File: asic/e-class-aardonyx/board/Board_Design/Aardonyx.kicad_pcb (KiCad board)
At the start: 4 copper layers, 311 parts, among them J1 USB_B_6PIN, J10 Conn_1x6_F, J11 Conn_1x6_F, J12 Conn_1x3_M, J13 Conn_1x8_F, J14 Conn_1x6_F, J15 Conn_1x10, J16 Conn_1x8_F, J17 USB_OTG, J18 Conn_1x3_M, J19 Conn_1x3_M, J2 Conn_1x8, J3 Conn_1x3_M, J4 Conn_1x4, J5 PJ-202H PWRJACK, J6 Conn_1x3_M, J7 Conn_1x4, J8 Conn_1x3_M, J9 Conn_1x8, Q1 FDN339AN, SW1 SW_SPST, SW2 FSM2JSMAATR, SW3 SW_DIP_x03, U1 FT2232H, U10 TPS7A7002DDAR, U11 ADM1085, U12 ADM1085, U13 TPS7A7002DDAR, U14 74AUP1G09GW, U15 SKT32E, U16 93LC56BT-I_OT, U2 IS42S32160F-TSOP2, U3 CDCE913PW, U4 TPS54627DDAR, U5 CAT24M01WI-GT3, U6 IS25LP256x-xM, U7 ADC128S102CIMTX/NOPB, U8 LSF0108PWR, U9 LSF0108PWR, Y1 12MHz, Y2 27MHz

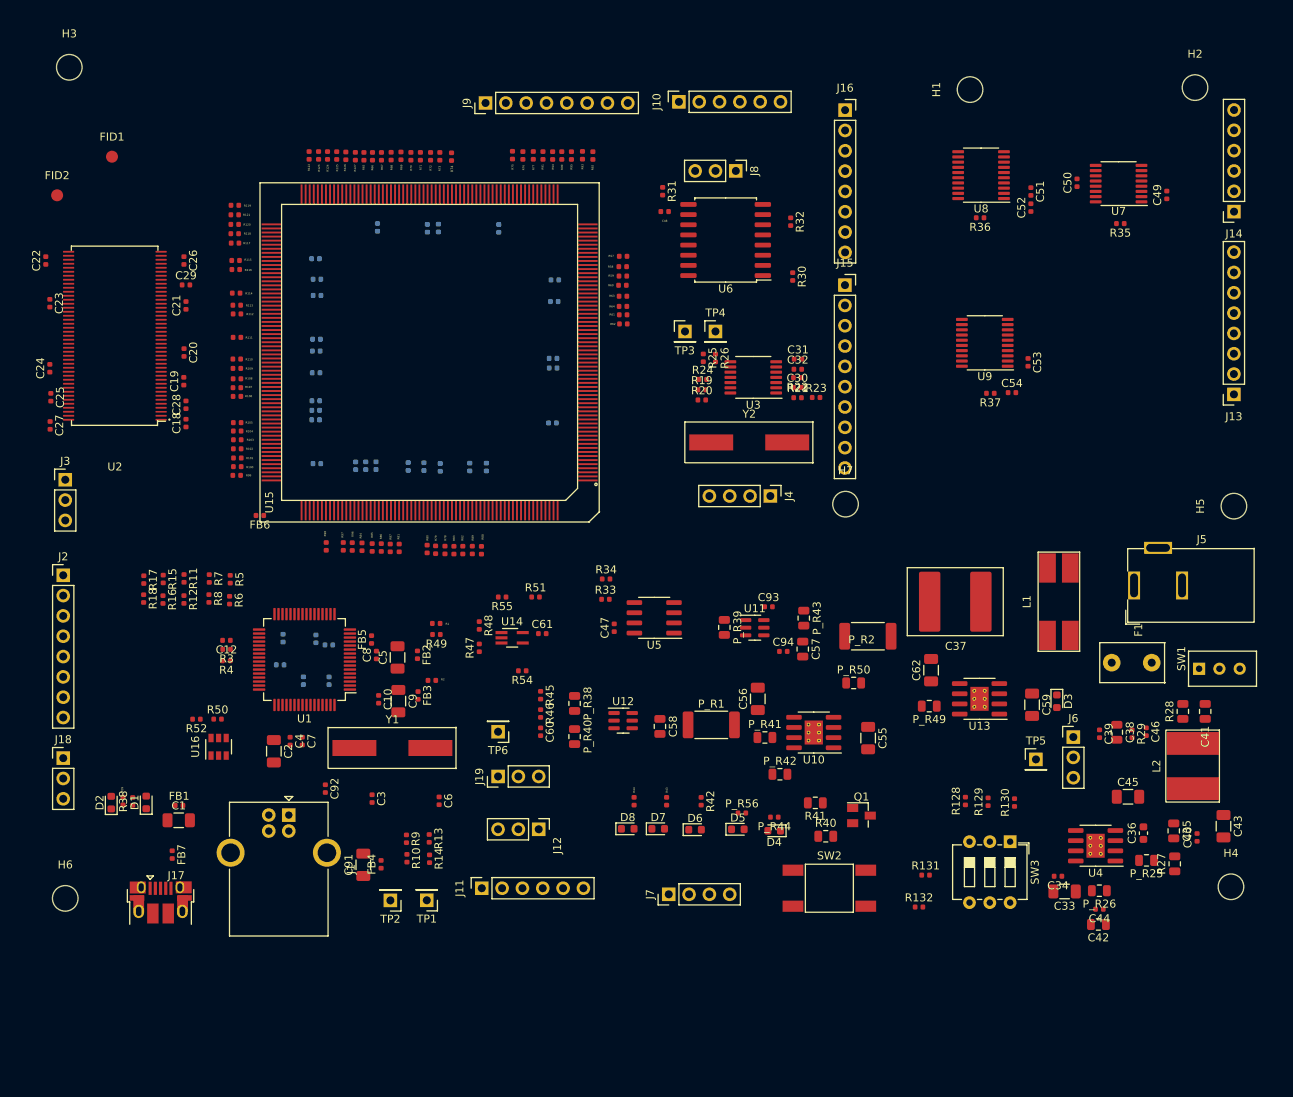
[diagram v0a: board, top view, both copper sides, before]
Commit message: minimize pcb size
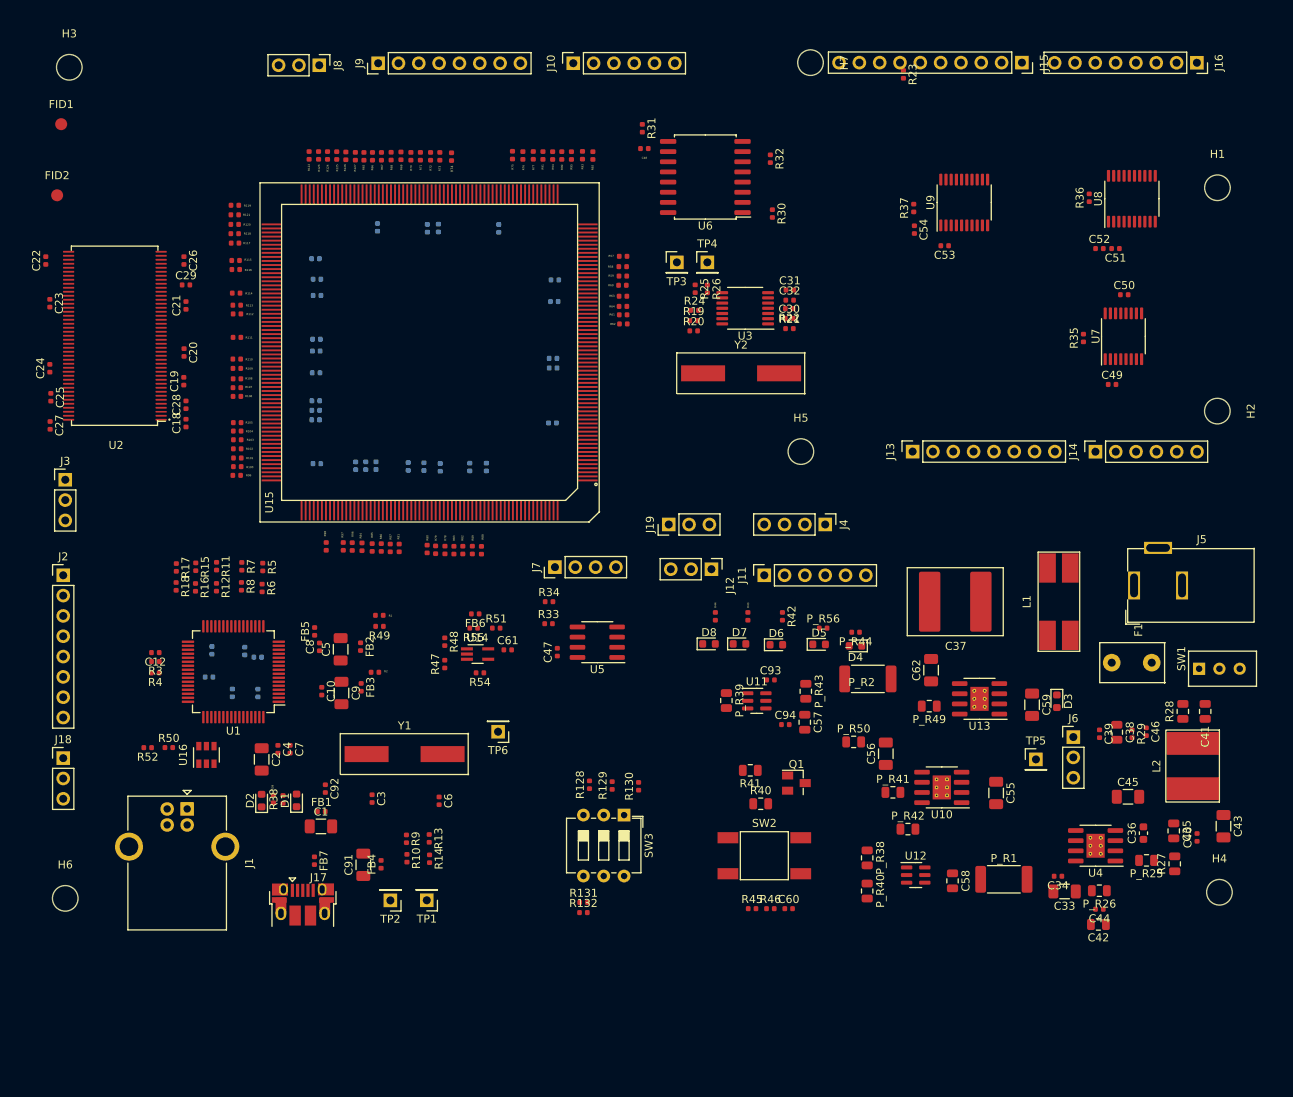
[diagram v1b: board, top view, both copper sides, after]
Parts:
- moved H7 55.4 mm to (222.4, 51.0), turned to 270 degrees
- moved H5 54.6 mm to (221.2, 99.6), turned to 0 degrees
- moved J8 53.7 mm to (161.0, 51.3)
- moved J11 52.7 mm to (216.7, 115.1)
- moved SW3 48.4 mm to (199.1, 145.0)
- moved R129 47.0 mm to (197.7, 141.3)
- moved R130 47.0 mm to (201.0, 141.4)
- moved R128 47.0 mm to (194.8, 141.2)
- moved J16 44.4 mm to (270.7, 51.0), turned to 270 degrees
- moved J7 43.3 mm to (190.5, 114.0)
- moved R131 42.9 mm to (194.1, 156.0)
- moved R132 42.0 mm to (194.1, 157.2)
- moved R23 41.8 mm to (234.1, 52.5), turned to 270 degrees
- moved U12 41.4 mm to (235.6, 152.5)
- moved P_R1 41.4 mm to (246.6, 153.1)
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
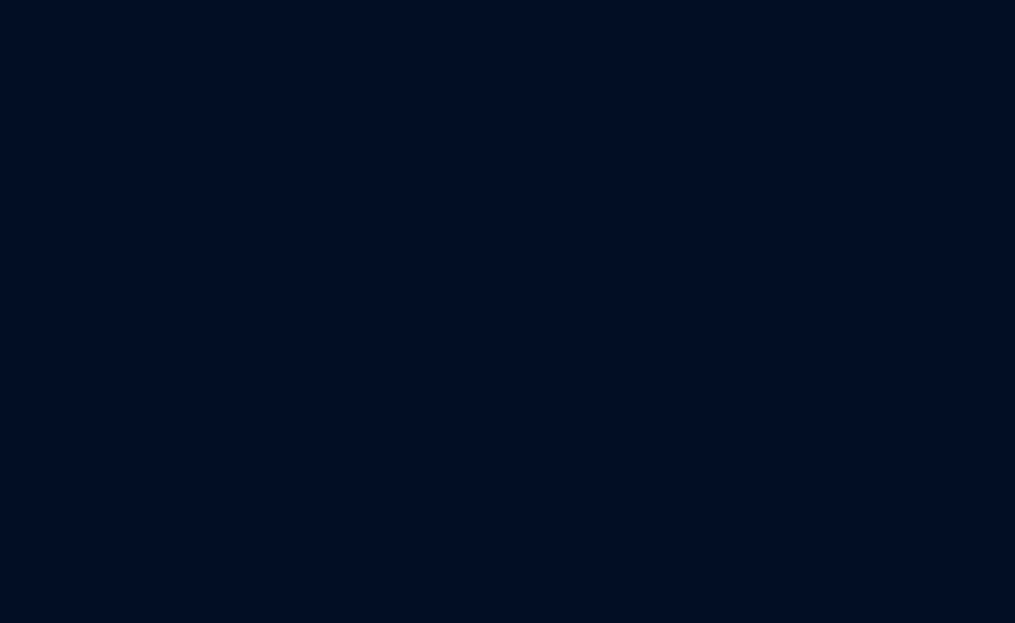
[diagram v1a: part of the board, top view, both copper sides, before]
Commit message: Updating footprint for test points
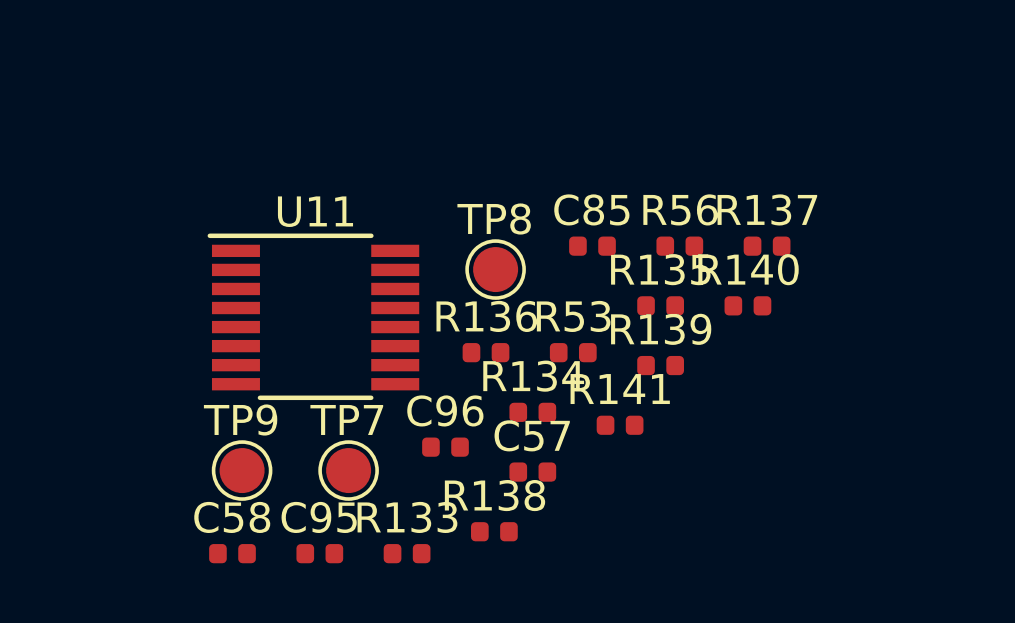
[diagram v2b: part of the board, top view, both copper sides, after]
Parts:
- added C57: 0.1UF,0402, Capacitor_SMD:C_0402_1005Metric, F.Cu at (160.5, 175.3)
- added C58: 0.1UF,0402, Capacitor_SMD:C_0402_1005Metric, F.Cu at (150.5, 178.0)
- added C85: 0.1UF,0402, Capacitor_SMD:C_0402_1005Metric, F.Cu at (162.5, 167.7)
- added C95: 0.1UF,0402, Capacitor_SMD:C_0402_1005Metric, F.Cu at (153.4, 178.0)
- added C96: 0.1UF,0402, Capacitor_SMD:C_0402_1005Metric, F.Cu at (157.6, 174.4)
- added R133: 4.7KE,0402, Resistor_SMD:R_0402_1005Metric, F.Cu at (156.3, 178.0)
- added R134: 1.2kE, 0402, Resistor_SMD:R_0402_1005Metric, F.Cu at (160.5, 173.3)
- added R135: 1.2kE, 0402, Resistor_SMD:R_0402_1005Metric, F.Cu at (164.8, 169.7)
- added R136: 4.7KE,0402, Resistor_SMD:R_0402_1005Metric, F.Cu at (159.0, 171.3)
- added R137: 10KE,0402, Resistor_SMD:R_0402_1005Metric, F.Cu at (168.3, 167.7)
- added R138: 10KE,0402, Resistor_SMD:R_0402_1005Metric, F.Cu at (159.2, 177.2)
- added R139: 10KE,0402, Resistor_SMD:R_0402_1005Metric, F.Cu at (164.8, 171.7)
- added R140: 10KE,0402, Resistor_SMD:R_0402_1005Metric, F.Cu at (167.7, 169.7)
- added R141: 10KE,0402, Resistor_SMD:R_0402_1005Metric, F.Cu at (163.4, 173.7)
- added R53: 4.7KE,0402, Resistor_SMD:R_0402_1005Metric, F.Cu at (161.9, 171.3)
- added R56: 3.3kE, 0402, Resistor_SMD:R_0402_1005Metric, F.Cu at (165.4, 167.7)
- added TP7: OUT3, TestPoint:TestPoint_Pad_D1.5mm, F.Cu at (154.4, 175.2)
- added TP8: OUT4, TestPoint:TestPoint_Pad_D1.5mm, F.Cu at (159.3, 168.5)
- added TP9: POWER_GOOD, TestPoint:TestPoint_Pad_D1.5mm, F.Cu at (150.8, 175.2)
- added U11: ADM1186, Package_SO:QSOP-16_3.9x4.9mm_P0.635mm, F.Cu at (153.3, 170.1)
- R19, R20, R21, R22, R23, R45: value 4.7KE, 0402 -> 4.7KE,0402
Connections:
- R49 pad 1: /ftdi/RESET -> /RESET
- R54 pad 2: /power_2/RESET -> /RESET
- R55 pad 2: /power_2/RESET -> /RESET
- U15 pad 24: /power_2/RESET -> /RESET

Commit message: add bom & updated component
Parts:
- R40, R41: footprint Resistor_SMD:R_0805_2012Metric -> Resistor_SMD:R_0402_1005Metric
- TP1, TP2, TP3, TP4, TP5, TP6: footprint Connector_PinHeader_2.54mm:PinHeader_1x01_P2.54mm_Vertical -> TestPoint:TestPoint_Pad_D1.5mm
- moved C42 44.9 mm to (234.9, 120.4)
- moved R139 41.1 mm to (192.0, 141.0)
- moved C44 41.0 mm to (235.5, 122.9)
- moved R53 40.6 mm to (188.0, 140.3)
- moved C85 40.1 mm to (188.9, 137.5)
- moved R135 40.1 mm to (191.2, 139.5)
- moved R137 40.1 mm to (194.8, 137.5)
- moved R140 40.1 mm to (194.1, 139.5)
- moved R56 40.1 mm to (191.8, 137.5)
- moved R134 39.4 mm to (192.3, 149.9)
- moved U11 39.4 mm to (185.0, 146.7)
- moved C57 39.4 mm to (192.3, 151.9)
- moved C58 39.4 mm to (182.3, 154.6)
- moved C95 39.4 mm to (185.2, 154.6)
- moved C96 39.4 mm to (189.4, 151.1)
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
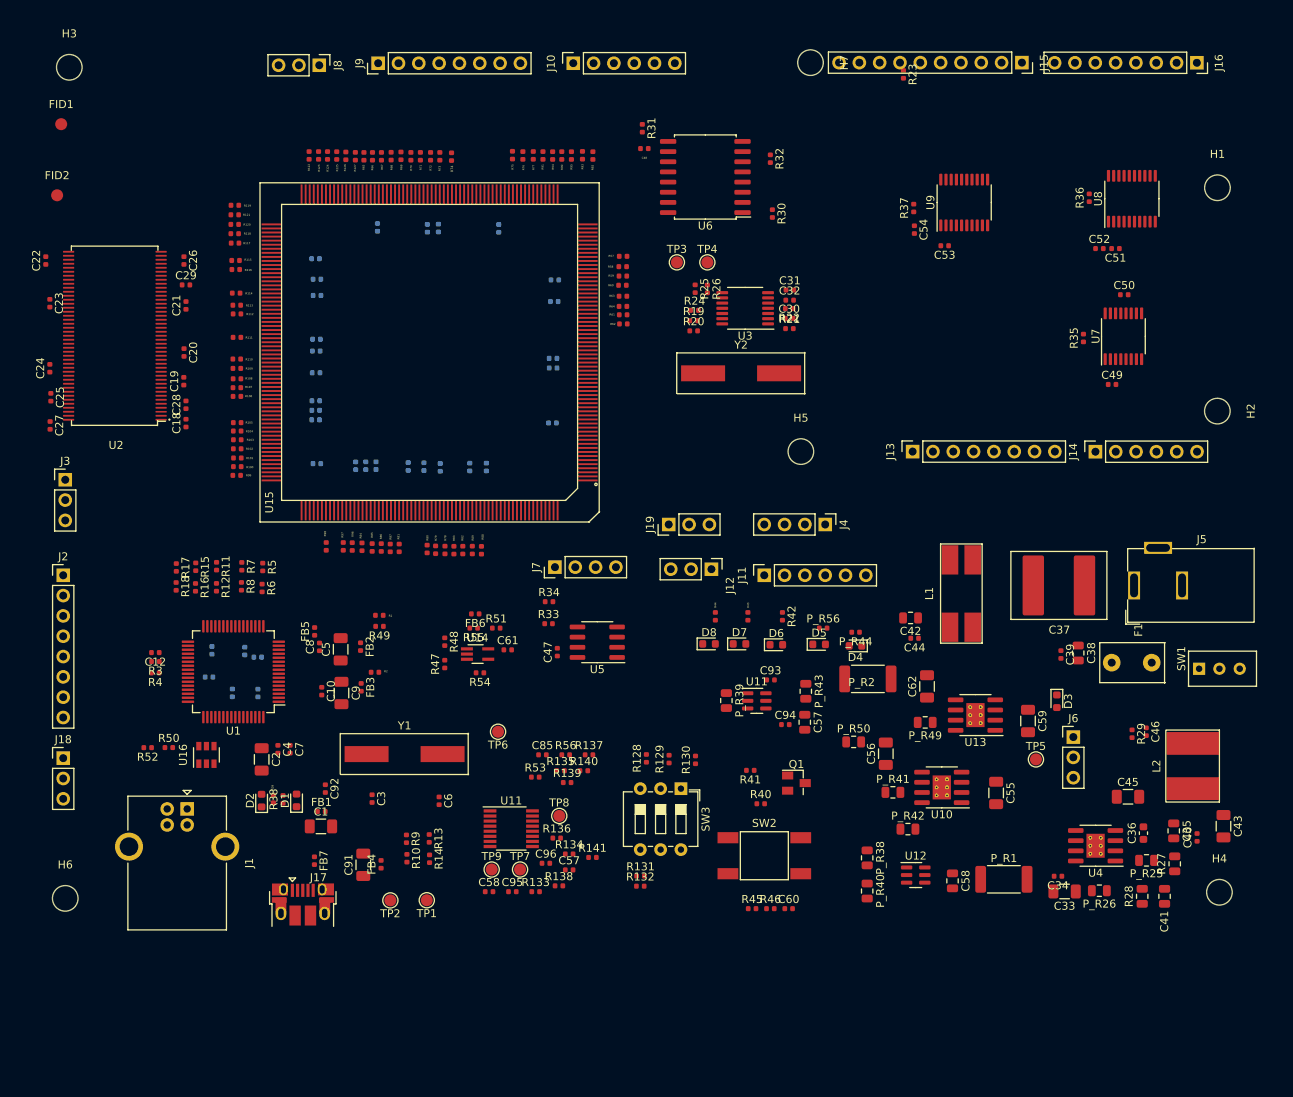
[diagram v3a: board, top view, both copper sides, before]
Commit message: Updating placements
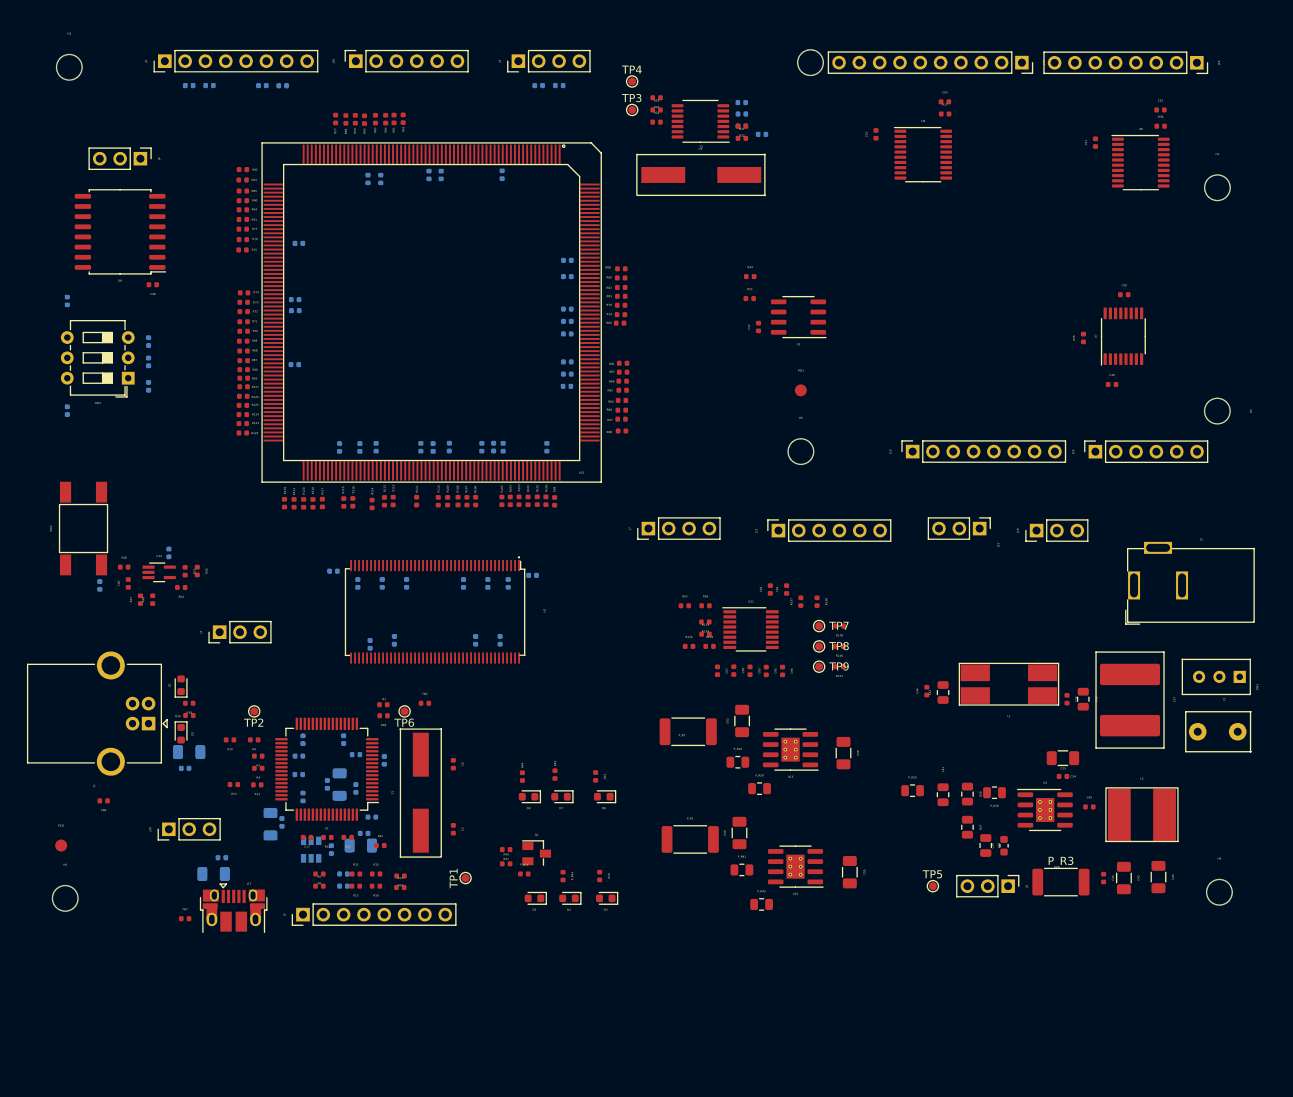
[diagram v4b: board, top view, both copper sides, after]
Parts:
- removed the C57 at (221.7, 133.4)
- removed the C58 at (240.2, 153.3)
- removed P_R38, P_R43: 10KE,0805, Resistor_SMD:R_0805_2012Metric
- removed P_R39, P_R40: 0E, 0805, Resistor_SMD:R_0805_2012Metric
- removed the U11 at (215.7, 130.8)
- removed U12: ADM1085, Package_SO:SC-74-6_1.5x2.9mm_P0.95mm
- added P_R3: 0.02E,2512, Resistor_SMD:R_2512_6332Metric, F.Cu at (253.7, 153.4)
- added R142: 10KE,0402, Resistor_SMD:R_0402_1005Metric, B.Cu at (147.3, 53.8)
- C1, C10, C12, C18, C19, C2, C20, C21, C22, C23, C24, C25, C26, C27, C28, C29, C30, C31, C32, C4, C5, C61, C7, C8, C9, C91, C92, FB1, FB3, FB4, R128, R129, R130, R131, R132, R19, R2, R20, R23, R30, R31, R32, R45, R7, R8, U16: moved to B.Cu
- C17: moved to F.Cu
- TP1, TP2, TP3, TP4, TP5, TP6, TP7, TP8, TP9: footprint TestPoint:TestPoint_Pad_D1.5mm -> TestPoint:TestPoint_Pad_D1.0mm
- moved R131 101.5 mm to (129.5, 80.8), turned to 270 degrees
- moved FID1 98.3 mm to (221.2, 91.9)
- moved SW2 94.4 mm to (131.6, 109.2), turned to 0 degrees
- moved R132 93.1 mm to (129.5, 94.5), turned to 90 degrees
- moved C60 92.0 mm to (137.2, 116.1), turned to 90 degrees
- moved R46 91.4 mm to (136.7, 114.0)
- moved R45 91.0 mm to (133.6, 116.3), turned to 90 degrees
- moved SW3 86.1 mm to (137.2, 90.4), turned to 180 degrees
- moved R130 82.8 mm to (139.7, 91.4), turned to 270 degrees
- moved R129 81.8 mm to (139.7, 88.4)
- moved FID2 81.3 mm to (128.8, 148.8)
- moved R128 81.2 mm to (139.7, 85.9), turned to 270 degrees
- moved U6 73.5 mm to (136.1, 72.1)
- moved R32 73.2 mm to (144.8, 53.8), turned to 180 degrees
- moved J4 69.5 mm to (185.9, 50.8), turned to 90 degrees
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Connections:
- C11 pad 1: ~ -> VCORE_FTDI
- C12 pad 1: ~ -> VCORE_FTDI
- C13 pad 1: ~ -> VCORE_FTDI
- C2 pad 1: ~ -> VCORE_FTDI
- C2 pad 2: Net-(C2-Pad2) -> GND
- C4 pad 1: ~ -> VCORE_FTDI
- C4 pad 2: Net-(C2-Pad2) -> GND
- C41 pad 1: ~ -> VCC5V
- C43 pad 1: ~ -> VCC5V
- C45 pad 1: ~ -> VCC5V
- C46 pad 1: ~ -> VCC5V
- C7 pad 1: V3P3 -> GND
- C7 pad 2: Net-(C2-Pad2) -> V3P3
- FB1 pad 2: ~ -> VBUS_USB2
- FB4 pad 2: ~ -> VBUS_USB1
- J18 pad 1: ~ -> VBUS_USB1
- J18 pad 3: ~ -> VBUS_USB2
- J6 pad 1: ~ -> Net-(J6-Pad1)
- L2 pad 2: ~ -> VCC5V
- R28 pad 1: ~ -> VCC5V
- U1 pad 12: ~ -> VCORE_FTDI
- U1 pad 37: ~ -> VCORE_FTDI
- U1 pad 49: ~ -> VCORE_FTDI
- U1 pad 64: ~ -> VCORE_FTDI
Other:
- rule trace_min: 0.2 -> 0.2032

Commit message: track update0
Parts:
- moved H3 2.31 mm to (127.9, 50.2)
- moved H6 0.83 mm to (128.7, 156.0)
- turned C36 to 270 degrees
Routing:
- net GND: track 0.00 -> 76.5 mm, vias 0 -> 3
- net VCC5V: track 0.00 -> 49.6 mm
- net ~: track 0.00 -> 27.6 mm
- net Net-(C37-Pad1): track 0.00 -> 23.5 mm
- net Net-(J5-Pad1): track 0.00 -> 18.6 mm
- net Net-(P_R25-Pad2): track 0.00 -> 15.5 mm
- net Net-(C41-Pad2): track 0.00 -> 13.1 mm
- net Net-(F1-Pad2): track 0.00 -> 8.86 mm
- net Net-(C40-Pad2): track 0.00 -> 8.12 mm
- net Net-(C35-Pad1): track 0.00 -> 6.08 mm
- net Net-(J6-Pad1): track 0.00 -> 4.05 mm
- net Net-(C36-Pad1): track 0.00 -> 3.80 mm
- net Net-(C40-Pad1): track 0.00 -> 2.67 mm
- added copper zone on F.Cu, net GND
- added copper zone on In1.Cu, net GND
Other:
- board outline added: 157.5 x 117.3 mm
